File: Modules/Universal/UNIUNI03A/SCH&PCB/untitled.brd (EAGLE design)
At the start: 20.2 x 60.8 mm, 5 parts, among them X1 SROUB3M, X2 SROUB3M, X3 SROUB3M, X4 SROUB3M

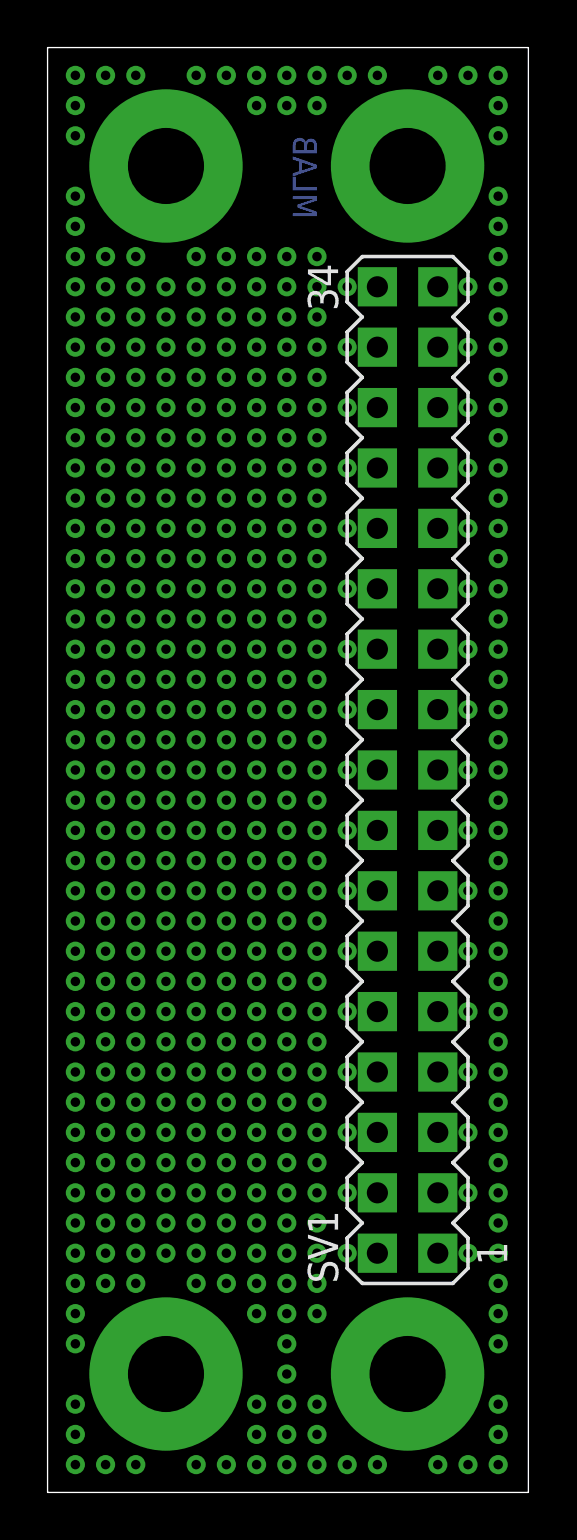
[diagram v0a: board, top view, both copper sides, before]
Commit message: 
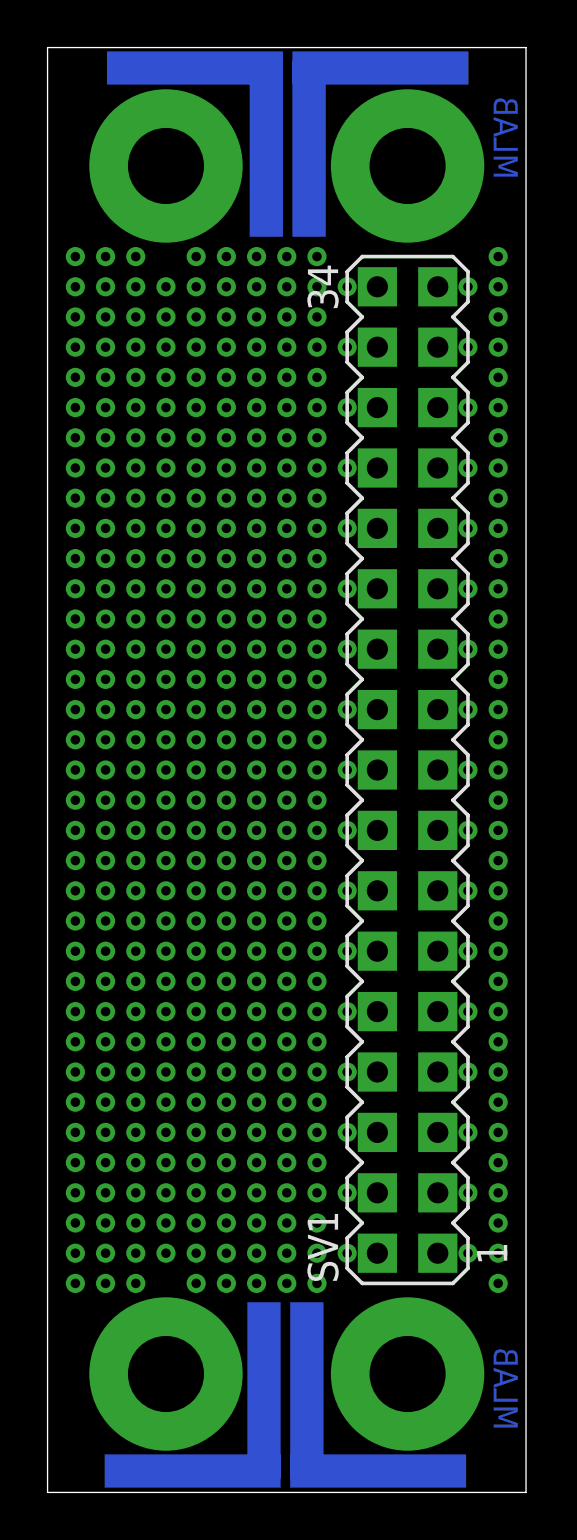
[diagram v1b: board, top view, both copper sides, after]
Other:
- board size 20.2 x 60.8 mm -> 20.1 x 60.8 mm
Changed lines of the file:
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@@
 <setting verticaltext="up"/>
 </settings>
-<grid distance="0.05" unitdist="inch" unit="mm" style="lines" multiple="1" display="no" altdistance="0.025" altunitdist="inch" altunit="inch"/>
+<grid distance="0.1" unitdist="mm" unit="mm" style="lines" multiple="1" display="no" altdistance="0.025" altunitdist="inch" altunit="inch"/>
 <layers>
 <layer number="1" name="Top" color="4" fill="1" visible="yes" active="yes"/>
@@
 <board>
 <plain>
-<wire x1="0.1" y1="0.1" x2="20.32" y2="0.1" width="0" layer="20"/>
-<wire x1="20.32" y1="0.1" x2="20.32" y2="60.86" width="0" layer="20"/>
-<wire x1="20.32" y1="60.86" x2="0.1" y2="60.86" width="0" layer="20"/>
+<wire x1="0.1" y1="0.1" x2="20.22" y2="0.1" width="0" layer="20"/>
+<wire x1="20.22" y1="0.1" x2="20.22" y2="60.86" width="0" layer="20"/>
+<wire x1="20.22" y1="60.86" x2="0.1" y2="60.86" width="0" layer="20"/>
 <wire x1="0.1" y1="60.86" x2="0.1" y2="0.1" width="0" layer="20"/>
-<text x="11.43" y="57.15" size="1.016" layer="16" rot="MR270">MLAB</text>
+<text x="18.86" y="55.31" size="1.016" layer="16" rot="MR90">MLAB</text>
+<text x="18.86" y="2.71" size="1.016" layer="16" rot="MR90">MLAB</text>
+<rectangle x1="8.6" y1="52.9" x2="10" y2="60.3" layer="16"/>
+<rectangle x1="10.4" y1="52.9" x2="11.8" y2="60.3" layer="16"/>
+<rectangle x1="13.4" y1="56.3" x2="14.8" y2="63.7" layer="16" rot="R90"/>
+<rectangle x1="5.6" y1="56.3" x2="7" y2="63.7" layer="16" rot="R270"/>
+<rectangle x1="10.3" y1="0.7" x2="11.7" y2="8.1" layer="16" rot="R180"/>
+<rectangle x1="8.5" y1="0.7" x2="9.9" y2="8.1" layer="16" rot="R180"/>
+<rectangle x1="5.5" y1="-2.7" x2="6.9" y2="4.7" layer="16" rot="R270"/>
+<rectangle x1="13.3" y1="-2.7" x2="14.7" y2="4.7" layer="16" rot="R90"/>
 </plain>
 <attributes>
@@
 <via x="1.27" y="52.07" extent="1-16" drill="0.4" shape="square"/>
 </signal>
-<signal name="N$331">
-<via x="8.89" y="7.62" extent="1-16" drill="0.4" shape="square"/>
-</signal>
-<signal name="N$332">
-<via x="10.16" y="7.62" extent="1-16" drill="0.4" shape="square"/>
-</signal>
-<signal name="N$333">
-<via x="11.43" y="7.62" extent="1-16" drill="0.4" shape="square"/>
-</signal>
-<signal name="N$334">
-<via x="10.16" y="6.35" extent="1-16" drill="0.4" shape="square"/>
-</signal>
-<signal name="N$335">
-<via x="10.16" y="5.08" extent="1-16" drill="0.4" shape="square"/>
-</signal>
-<signal name="N$336">
-<via x="10.16" y="3.81" extent="1-16" drill="0.4" shape="square"/>
-</signal>
-<signal name="N$337">
-<via x="8.89" y="3.81" extent="1-16" drill="0.4" shape="square"/>
-</signal>
-<signal name="N$338">
-<via x="11.43" y="3.81" extent="1-16" drill="0.4" shape="square"/>
-</signal>
-<signal name="N$339">
-<via x="11.43" y="2.54" extent="1-16" drill="0.4" shape="square"/>
-</signal>
-<signal name="N$340">
-<via x="10.16" y="2.54" extent="1-16" drill="0.4" shape="square"/>
-</signal>
-<signal name="N$341">
-<via x="8.89" y="2.54" extent="1-16" drill="0.4" shape="square"/>
-</signal>
-<signal name="N$342">
-<via x="7.62" y="1.27" extent="1-16" drill="0.4" shape="square"/>
-</signal>
-<signal name="N$343">
-<via x="8.89" y="1.27" extent="1-16" drill="0.4" shape="square"/>
-</signal>
-<signal name="N$344">
-<via x="10.16" y="1.27" extent="1-16" drill="0.4" shape="square"/>
-</signal>
-<signal name="N$345">
-<via x="11.43" y="1.27" extent="1-16" drill="0.4" shape="square"/>
-</signal>
-<signal name="N$346">
-<via x="12.7" y="1.27" extent="1-16" drill="0.4" shape="square"/>
-</signal>
-<signal name="N$347">
-<via x="13.97" y="1.27" extent="1-16" drill="0.4" shape="square"/>
-</signal>
-<signal name="N$349">
-<via x="16.51" y="1.27" extent="1-16" drill="0.4" shape="square"/>
-</signal>
-<signal name="N$350">
-<via x="17.78" y="1.27" extent="1-16" drill="0.4" shape="square"/>
-</signal>
-<signal name="N$351">
-<via x="19.05" y="1.27" extent="1-16" drill="0.4" shape="square"/>
-</signal>
-<signal name="N$352">
-<via x="19.05" y="2.54" extent="1-16" drill="0.4" shape="square"/>
-</signal>
-<signal name="N$353">
-<via x="19.05" y="3.81" extent="1-16" drill="0.4" shape="square"/>
-</signal>
-<signal name="N$355">
-<via x="19.05" y="6.35" extent="1-16" drill="0.4" shape="square"/>
-</signal>
-<signal name="N$356">
-<via x="19.05" y="7.62" extent="1-16" drill="0.4" shape="square"/>
-</signal>
 <signal name="N$357">
 <via x="19.05" y="8.89" extent="1-16" drill="0.4" shape="square"/>
 </signal>
-<signal name="N$358">
-<via x="6.35" y="1.27" extent="1-16" drill="0.4" shape="square"/>
-</signal>
-<signal name="N$360">
-<via x="3.81" y="1.27" extent="1-16" drill="0.4" shape="square"/>
-</signal>
-<signal name="N$361">
-<via x="2.54" y="1.27" extent="1-16" drill="0.4" shape="square"/>
-</signal>
-<signal name="N$362">
-<via x="1.27" y="1.27" extent="1-16" drill="0.4" shape="square"/>
-</signal>
-<signal name="N$363">
-<via x="1.27" y="3.81" extent="1-16" drill="0.4" shape="square"/>
-</signal>
-<signal name="N$364">
-<via x="1.27" y="6.35" extent="1-16" drill="0.4" shape="square"/>
-</signal>
-<signal name="N$365">
-<via x="1.27" y="7.62" extent="1-16" drill="0.4" shape="square"/>
-</signal>
-<signal name="N$367">
-<via x="1.27" y="2.54" extent="1-16" drill="0.4" shape="square"/>
-</signal>
-<signal name="N$368">
-<via x="1.27" y="53.34" extent="1-16" drill="0.4" shape="square"/>
-</signal>
-<signal name="N$369">
-<via x="1.27" y="54.61" extent="1-16" drill="0.4" shape="square"/>
-</signal>
-<signal name="N$370">
-<via x="1.27" y="57.15" extent="1-16" drill="0.4" shape="square"/>
-</signal>
-<signal name="N$372">
-<via x="1.27" y="58.42" extent="1-16" drill="0.4" shape="square"/>
-</signal>
-<signal name="N$373">
-<via x="1.27" y="59.69" extent="1-16" drill="0.4" shape="square"/>
-</signal>
-<signal name="N$374">
-<via x="2.54" y="59.69" extent="1-16" drill="0.4" shape="square"/>
-</signal>
-<signal name="N$375">
-<via x="3.81" y="59.69" extent="1-16" drill="0.4" shape="square"/>
-</signal>
-<signal name="N$376">
-<via x="6.35" y="59.69" extent="1-16" drill="0.4" shape="square"/>
-</signal>
-<signal name="N$378">
-<via x="7.62" y="59.69" extent="1-16" drill="0.4" shape="square"/>
-</signal>
-<signal name="N$379">
-<via x="8.89" y="59.69" extent="1-16" drill="0.4" shape="square"/>
-</signal>
-<signal name="N$380">
-<via x="11.43" y="59.69" extent="1-16" drill="0.4" shape="square"/>
-</signal>
-<signal name="N$381">
-<via x="10.16" y="59.69" extent="1-16" drill="0.4" shape="square"/>
-</signal>
-<signal name="N$382">
-<via x="12.7" y="59.69" extent="1-16" drill="0.4" shape="square"/>
-</signal>
-<signal name="N$384">
-<via x="13.97" y="59.69" extent="1-16" drill="0.4" shape="square"/>
-</signal>
-<signal name="N$348">
-<via x="16.51" y="59.69" extent="1-16" drill="0.4" shape="square"/>
-</signal>
-<signal name="N$359">
-<via x="19.05" y="59.69" extent="1-16" drill="0.4" shape="square"/>
-</signal>
-<signal name="N$377">
-<via x="17.78" y="59.69" extent="1-16" drill="0.4" shape="square"/>
-</signal>
 <signal name="N$383">
 <via x="19.05" y="10.16" extent="1-16" drill="0.4" shape="square"/>
@@
 <via x="17.78" y="50.8" extent="1-16" drill="0.4" shape="square"/>
 </signal>
-<signal name="N$406">
-<via x="19.05" y="58.42" extent="1-16" drill="0.4" shape="square"/>
-</signal>
-<signal name="N$407">
-<via x="19.05" y="57.15" extent="1-16" drill="0.4" shape="square"/>
-</signal>
-<signal name="N$354">
-<via x="19.05" y="54.61" extent="1-16" drill="0.4" shape="square"/>
-</signal>
-<signal name="N$366">
-<via x="19.05" y="53.34" extent="1-16" drill="0.4" shape="square"/>
-</signal>
 <signal name="N$409">
 <via x="19.05" y="52.07" extent="1-16" drill="0.4" shape="square"/>
@@
 <via x="19.05" y="41.91" extent="1-16" drill="0.4" shape="square"/>
 </signal>
-<signal name="N$436">
-<via x="8.89" y="58.42" extent="1-16" drill="0.4" shape="square"/>
-</signal>
-<signal name="N$437">
-<via x="11.43" y="58.42" extent="1-16" drill="0.4" shape="square"/>
-</signal>
-<signal name="N$438">
-<via x="10.16" y="58.42" extent="1-16" drill="0.4" shape="square"/>
-</signal>
 </signals>
